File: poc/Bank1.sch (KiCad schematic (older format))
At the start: 6 parts

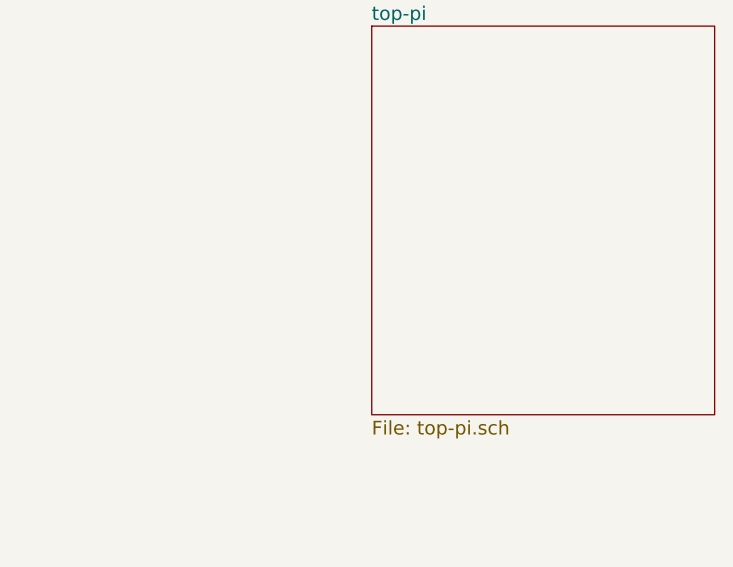
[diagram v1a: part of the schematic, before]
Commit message: LAN9512 Ethernet wiring
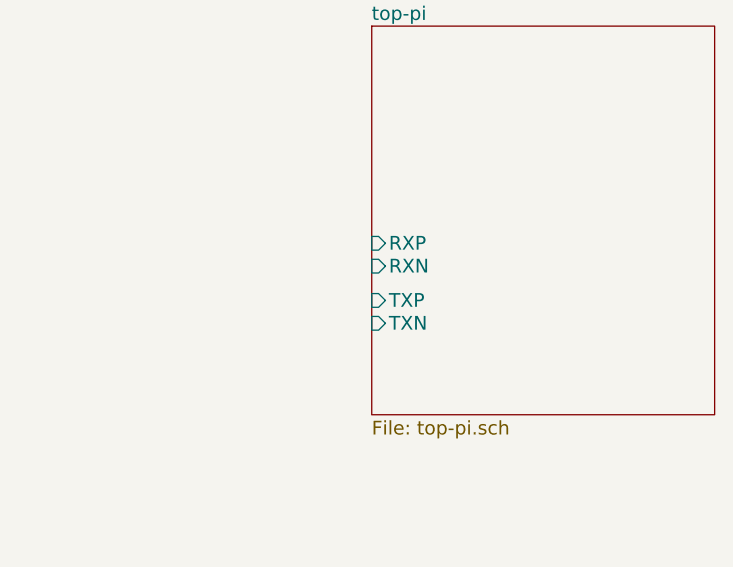
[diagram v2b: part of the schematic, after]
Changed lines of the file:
@@
 F0 "top-pi" 60
 F1 "top-pi.sch" 60
+F2 "RXP" I L 7150 2300 60
+F3 "RXN" I L 7150 2400 60
+F4 "TXP" I L 7150 2550 60
+F5 "TXN" I L 7150 2650 60
 $EndSheet
 $Comp

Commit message: Upgrade to newer kicad
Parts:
- C? (x4): symbol C_Small -> poc-rescue:C_Small
- T?: symbol DS75 -> ds75:DS75
- U?: symbol SC16IS752 -> sc16is752:SC16IS752
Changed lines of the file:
@@
-EESchema Schematic File Version 2
-LIBS:power
-LIBS:device
-LIBS:transistors
-LIBS:conn
-LIBS:linear
-LIBS:regul
-LIBS:74xx
-LIBS:cmos4000
-LIBS:adc-dac
-LIBS:memory
-LIBS:xilinx
-LIBS:microcontrollers
-LIBS:dsp
-LIBS:microchip
-LIBS:analog_switches
-LIBS:motorola
-LIBS:texas
-LIBS:intel
-LIBS:audio
-LIBS:interface
-LIBS:digital-audio
-LIBS:philips
-LIBS:display
-LIBS:cypress
-LIBS:siliconi
-LIBS:opto
-LIBS:atmel
-LIBS:contrib
-LIBS:valves
-LIBS:cm3l
-LIBS:LAN9512
-LIBS:usb_a_x2
-LIBS:CD74HC154
-LIBS:sc16is752
-LIBS:KSZ9897R
-LIBS:belfuse_gige
-LIBS:SAM4E
-LIBS:DP83867
-LIBS:ds75
+EESchema Schematic File Version 4
 LIBS:poc-cache
-EELAYER 25 0
+EELAYER 30 0
 EELAYER END
 $Descr A4 11693 8268
@@
 $EndSheet
 $Comp
-L DS75 T?
+L ds75:DS75 T?
 U 1 1 59918763
 P 2600 2150
@@
 $EndComp
 $Comp
-L SC16IS752 U?
+L sc16is752:SC16IS752 U?
 U 1 1 599187DB
 P 2550 3600
@@
 $EndComp
 $Comp
-L +3V3 #PWR055
+L power:+3V3 #PWR055
 U 1 1 59918878
 P 3300 2350
@@
 $EndComp
 $Comp
-L GND #PWR056
+L power:GND #PWR056
 U 1 1 599188CF
 P 2350 2650
@@
 $EndComp
 $Comp
-L +3V3 #PWR057
+L power:+3V3 #PWR057
 U 1 1 599188F9
 P 700 850
@@
 $EndComp
 $Comp
-L GND #PWR058
+L power:GND #PWR058
 U 1 1 59918954
 P 700 1050
@@
 $EndComp
 $Comp
-L C_Small C?
+L poc-rescue:C_Small C?
 U 1 1 5991896D
 P 900 950
@@
 $EndComp
 $Comp
-L C_Small C?
+L poc-rescue:C_Small C?
 U 1 1 599189C2
 P 1200 950
@@
 Place near\nDS75 VDD
 $Comp
-L GND #PWR059
+L power:GND #PWR059
 U 1 1 59918FD5
 P 2200 5200
@@
 $EndComp
 $Comp
-L +3V3 #PWR060
+L power:+3V3 #PWR060
 U 1 1 59919042
 P 2200 4600
@@
 $EndComp
 $Comp
-L +3V3 #PWR061
+L power:+3V3 #PWR061
 U 1 1 59919149
 P 700 1600
@@
 $EndComp
 $Comp
-L GND #PWR062
+L power:GND #PWR062
 U 1 1 5991914F
 P 700 1800
@@
 $EndComp
 $Comp
-L C_Small C?
+L poc-rescue:C_Small C?
 U 1 1 59919155
 P 900 1700
@@
 $EndComp
 $Comp
-L C_Small C?
+L poc-rescue:C_Small C?
 U 1 1 5991915B
 P 1200 1700

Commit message: wire SD card to cm3l
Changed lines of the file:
@@
 $EndComp
 Wire Wire Line
-	700  850  1200 850
+	700  850  900  850
 Wire Wire Line
-	1200 1050 700  1050
+	1200 1050 900  1050
 Connection ~ 900  850
 Connection ~ 900  1050
@@
 $EndComp
 Wire Wire Line
-	700  1600 1200 1600
+	700  1600 900  1600
 Wire Wire Line
-	1200 1800 700  1800
+	1200 1800 900  1800
 Connection ~ 900  1600
 Connection ~ 900  1800
@@
 Text Notes 2650 3600 0    60   ~ 0
 DUART
+Wire Wire Line
+	900  850  1200 850
+Wire Wire Line
+	900  1050 700  1050
+Wire Wire Line
+	900  1600 1200 1600
+Wire Wire Line
+	900  1800 700  1800
 $EndSCHEMATC
